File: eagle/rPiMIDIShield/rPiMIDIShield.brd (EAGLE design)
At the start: 56 x 85 mm, 9 parts

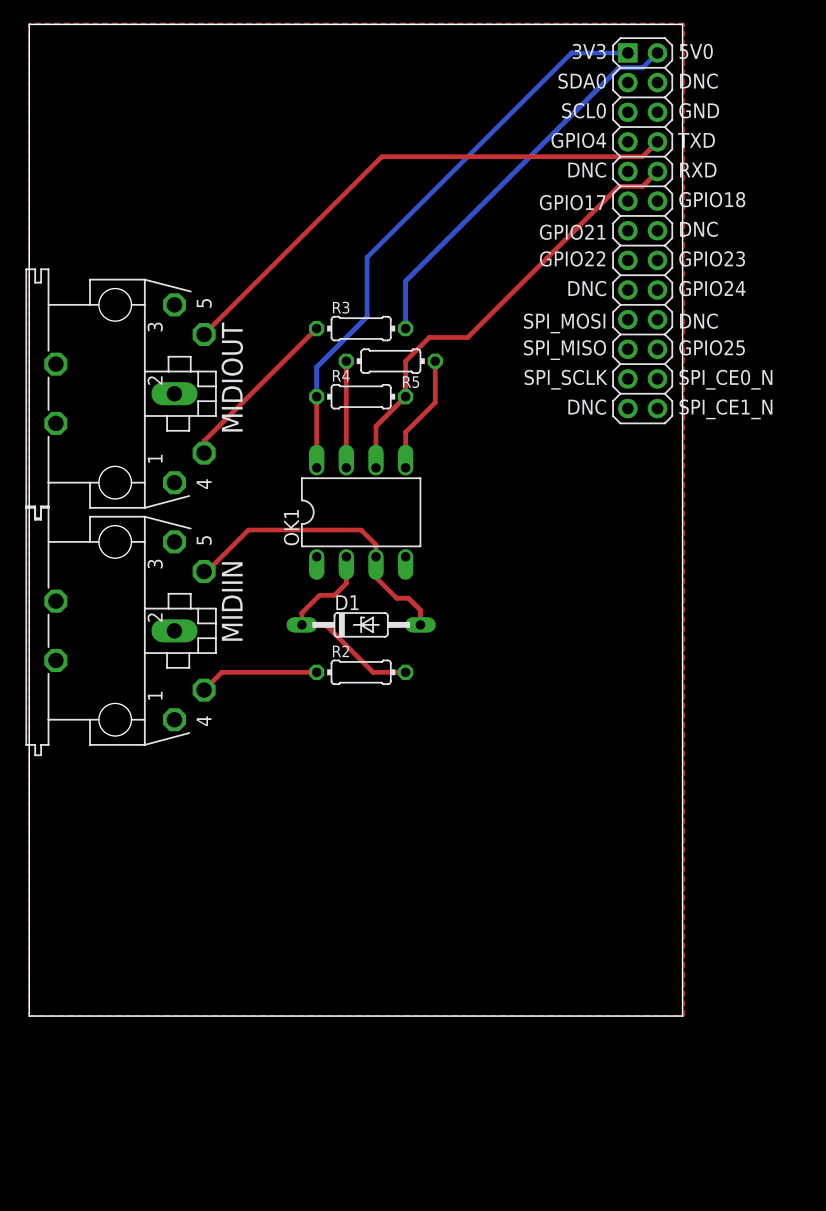
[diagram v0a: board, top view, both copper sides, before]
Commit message: Added GPIO headers to the rPI board
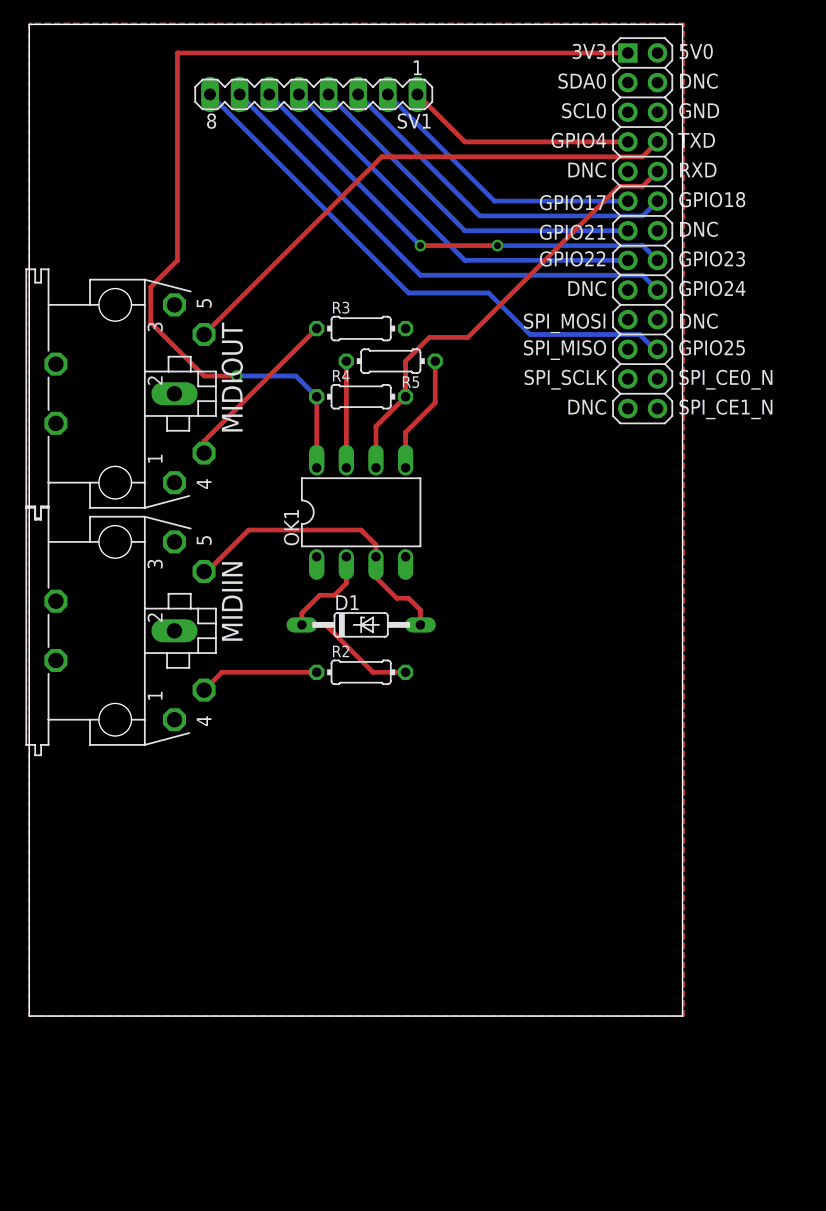
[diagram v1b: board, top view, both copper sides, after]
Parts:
- added SV1: (no value), con-lstb:MA08-1
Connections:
- net GPIO17: now also SV1.2
- net GPIO18: now also SV1.3
- net GPIO21: now also SV1.4
- net GPIO22: now also SV1.5
- net GPIO23: now also SV1.6
- net GPIO24: now also SV1.7
- net GPIO25: now also SV1.8
- net GPIO4: now also SV1.1
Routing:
- net GPIO25: track 0.00 -> 47.4 mm
- net GPIO24: track 0.00 -> 42.8 mm
- net GPIO23: track 0.00 -> 39.2 mm, vias 0 -> 2
- net 3.3V: track 49.2 -> 85.4 mm, vias 0 -> 1
- net GPIO22: track 0.00 -> 34.1 mm
- net 5.0V: track 33.8 -> 0.00 mm
- net GPIO18: track 0.00 -> 30.5 mm
- net GPIO21: track 0.00 -> 30.5 mm
- net GPIO17: track 0.00 -> 24.4 mm
- net GPIO4: track 0.00 -> 19.5 mm
- added copper zone on layer 16, net 5.0V
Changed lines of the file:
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@@
 <element name="R5" library="resistor" package="0204/7" value="1k" x="30.988" y="56.134" rot="R180"/>
 <element name="D1" library="diode" package="DO35Z10" value="1N821" x="28.448" y="33.528"/>
+<element name="SV1" library="con-lstb" package="MA08-1" value="" x="24.384" y="78.994" rot="R180">
+<attribute name="OC_NEWARK" value="unknown" x="24.384" y="78.994" size="1.778" layer="27" rot="R180" display="off"/>
+<attribute name="MPN" value="" x="24.384" y="78.994" size="1.778" layer="27" rot="R180" display="off"/>
+<attribute name="MF" value="" x="24.384" y="78.994" size="1.778" layer="27" rot="R180" display="off"/>
+<attribute name="OC_FARNELL" value="unknown" x="24.384" y="78.994" size="1.778" layer="27" rot="R180" display="off"/>
+</element>
 </elements>
 <signals>
 <signal name="GPIO17">
 <contactref element="U$1" pad="11"/>
+<contactref element="SV1" pad="2"/>
+<wire x1="51.308" y1="69.85" x2="39.878" y2="69.85" width="0.4064" layer="16"/>
+<wire x1="39.878" y1="69.85" x2="30.734" y2="78.994" width="0.4064" layer="16"/>
 </signal>
 <signal name="GPIO18">
 <contactref element="U$1" pad="12"/>
+<contactref element="SV1" pad="3"/>
+<wire x1="53.848" y1="69.85" x2="52.578" y2="68.58" width="0.4064" layer="16"/>
+<wire x1="52.578" y1="68.58" x2="38.608" y2="68.58" width="0.4064" layer="16"/>
+<wire x1="38.608" y1="68.58" x2="28.194" y2="78.994" width="0.4064" layer="16"/>
 </signal>
 <signal name="GPIO21">
 <contactref element="U$1" pad="13"/>
+<contactref element="SV1" pad="4"/>
+<wire x1="51.308" y1="67.31" x2="37.338" y2="67.31" width="0.4064" layer="16"/>
+<wire x1="37.338" y1="67.31" x2="25.654" y2="78.994" width="0.4064" layer="16"/>
 </signal>
 <signal name="GPIO22">
 <contactref element="U$1" pad="15"/>
+<contactref element="SV1" pad="5"/>
+<wire x1="51.308" y1="64.77" x2="37.338" y2="64.77" width="0.4064" layer="16"/>
+<wire x1="37.338" y1="64.77" x2="23.114" y2="78.994" width="0.4064" layer="16"/>
 </signal>
 <signal name="GPIO23">
 <contactref element="U$1" pad="16"/>
+<contactref element="SV1" pad="6"/>
+<wire x1="53.848" y1="64.77" x2="52.578" y2="66.04" width="0.4064" layer="16"/>
+<wire x1="52.578" y1="66.04" x2="40.132" y2="66.04" width="0.4064" layer="16"/>
+<via x="40.132" y="66.04" extent="1-16" drill="0.6" shape="square"/>
+<wire x1="40.132" y1="66.04" x2="33.528" y2="66.04" width="0.4064" layer="1"/>
+<via x="33.528" y="66.04" extent="1-16" drill="0.6" shape="square"/>
+<wire x1="33.528" y1="66.04" x2="20.574" y2="78.994" width="0.4064" layer="16"/>
 </signal>
 <signal name="GPIO24">
 <contactref element="U$1" pad="18"/>
+<contactref element="SV1" pad="7"/>
+<wire x1="53.848" y1="62.23" x2="52.578" y2="63.5" width="0.4064" layer="16"/>
+<wire x1="52.578" y1="63.5" x2="33.528" y2="63.5" width="0.4064" layer="16"/>
+<wire x1="33.528" y1="63.5" x2="18.034" y2="78.994" width="0.4064" layer="16"/>
 </signal>
 <signal name="GPIO25">
 <contactref element="U$1" pad="22"/>
+<contactref element="SV1" pad="8"/>
+<wire x1="53.848" y1="57.15" x2="53.594" y2="57.15" width="0.4064" layer="16"/>
+<wire x1="53.594" y1="57.15" x2="52.324" y2="58.42" width="0.4064" layer="16"/>
+<wire x1="52.324" y1="58.42" x2="42.926" y2="58.42" width="0.4064" layer="16"/>
+<wire x1="42.926" y1="58.42" x2="39.37" y2="61.976" width="0.4064" layer="16"/>
+<wire x1="39.37" y1="61.976" x2="32.512" y2="61.976" width="0.4064" layer="16"/>
+<wire x1="32.512" y1="61.976" x2="15.494" y2="78.994" width="0.4064" layer="16"/>
 </signal>
 <signal name="GPIO4">
 <contactref element="U$1" pad="7"/>
+<contactref element="SV1" pad="1"/>
+<wire x1="51.054" y1="74.93" x2="37.338" y2="74.93" width="0.4064" layer="1"/>
+<wire x1="37.338" y1="74.93" x2="33.274" y2="78.994" width="0.4064" layer="1"/>
+<wire x1="51.054" y1="74.93" x2="51.308" y2="74.93" width="0" layer="19" extent="1-1"/>
 </signal>
 <signal name="3.3V">
@@
 <contactref element="OK1" pad="8"/>
 <wire x1="24.638" y1="53.086" x2="24.638" y2="47.244" width="0.4064" layer="1"/>
-<wire x1="24.638" y1="53.086" x2="24.638" y2="55.626" width="0.4064" layer="16"/>
-<wire x1="24.638" y1="55.626" x2="28.956" y2="59.944" width="0.4064" layer="16"/>
-<wire x1="28.956" y1="59.944" x2="28.956" y2="65.024" width="0.4064" layer="16"/>
-<wire x1="28.956" y1="65.024" x2="46.482" y2="82.55" width="0.4064" layer="16"/>
-<wire x1="46.482" y1="82.55" x2="51.308" y2="82.55" width="0.4064" layer="16"/>
+<wire x1="51.308" y1="82.55" x2="12.7" y2="82.55" width="0.4064" layer="1"/>
+<wire x1="12.7" y1="82.55" x2="12.7" y2="64.77" width="0.4064" layer="1"/>
+<wire x1="12.7" y1="64.77" x2="10.414" y2="62.484" width="0.4064" layer="1"/>
+<wire x1="10.414" y1="62.484" x2="10.414" y2="59.436" width="0.4064" layer="1"/>
+<wire x1="10.414" y1="59.436" x2="14.986" y2="54.864" width="0.4064" layer="1"/>
+<wire x1="14.986" y1="54.864" x2="17.78" y2="54.864" width="0.4064" layer="1"/>
+<via x="17.78" y="54.864" extent="1-16" drill="0.6" shape="square"/>
+<wire x1="17.78" y1="54.864" x2="22.86" y2="54.864" width="0.4064" layer="16"/>
+<wire x1="22.86" y1="54.864" x2="24.638" y2="53.086" width="0.4064" layer="16"/>
 <wire x1="24.638" y1="47.244" x2="24.638" y2="46.99" width="0" layer="19" extent="1-1"/>
 </signal>
@@
 <contactref element="U$1" pad="2"/>
 <contactref element="R3" pad="2"/>
-<wire x1="53.848" y1="82.55" x2="52.578" y2="81.28" width="0.4064" layer="16"/>
-<wire x1="52.578" y1="81.28" x2="50.546" y2="81.28" width="0.4064" layer="16"/>
-<wire x1="50.546" y1="81.28" x2="32.258" y2="62.992" width="0.4064" layer="16"/>
-<wire x1="32.258" y1="62.992" x2="32.258" y2="58.928" width="0.4064" layer="16"/>
+<polygon width="0.4064" layer="16">
+<vertex x="0" y="85.09"/>
+<vertex x="0" y="0"/>
+<vertex x="56.134" y="0"/>
+<vertex x="56.134" y="85.09"/>
+<vertex x="0.254" y="85.09"/>
+</polygon>
 </signal>
 <signal name="GND">

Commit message: Modified the labels so they don't show up on silkscreen. Also moved all components within eagle's 'Approved Board Size'
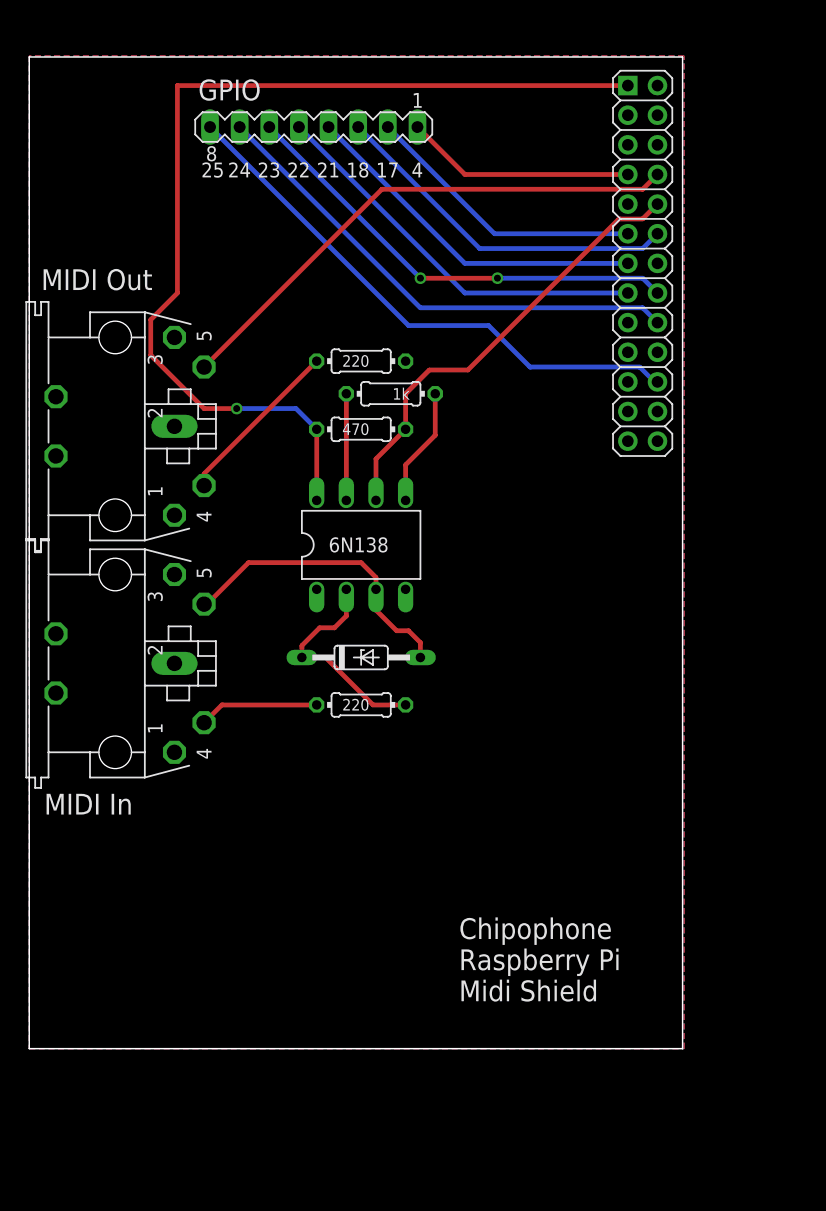
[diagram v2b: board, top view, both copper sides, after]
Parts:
- removed U$1: RASPBERRYPI_BB, microbuilder:RASBERRYPI_SHIELD
- added GPIO: RASPBERRYPI_BB, microbuilder:RASBERRYPI_SHIELD
- moved MIDIIN 2.79 mm to (7.37, 30.2)
- moved MIDIOUT 2.79 mm to (7.37, 50.5)
- moved D1 2.79 mm to (28.4, 30.7)
- moved OK1 2.79 mm to (28.4, 40.4)
- moved R2 2.79 mm to (28.4, 26.7)
- moved R3 2.79 mm to (28.4, 56.1)
- moved R4 2.79 mm to (28.4, 50.3)
- moved R5 2.79 mm to (31.0, 53.3)
- moved SV1 2.79 mm to (24.4, 76.2)
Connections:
- removed net PE: MIDIIN.PE, MIDIIN.PE@
- net 3.3V: now also GPIO.1; no longer U$1.1
- net 5.0V: now also GPIO.2; no longer U$1.2
- net GND: now also GPIO.6, MIDIIN.PE, MIDIIN.PE@, MIDIOUT.2; no longer U$1.6
- net GPIO17: now also GPIO.11; no longer U$1.11
- net GPIO18: now also GPIO.12; no longer U$1.12
- net GPIO21: now also GPIO.13; no longer U$1.13
- net GPIO22: now also GPIO.15; no longer U$1.15
- net GPIO23: now also GPIO.16; no longer U$1.16
- net GPIO24: now also GPIO.18; no longer U$1.18
- net GPIO25: now also GPIO.22; no longer U$1.22
- net GPIO4: now also GPIO.7; no longer U$1.7
- net MISO: now also GPIO.21; no longer U$1.21
- net MOSI: now also GPIO.19; no longer U$1.19
- net RXD: now also GPIO.10; no longer U$1.10
- net SCL: now also GPIO.5; no longer U$1.5
- net SCLK: now also GPIO.23; no longer U$1.23
- net SDA: now also GPIO.3; no longer U$1.3
- net SPI_CE0: now also GPIO.24; no longer U$1.24
- net SPI_CE1: now also GPIO.26; no longer U$1.26
- net TXD: now also GPIO.8; no longer U$1.8
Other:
- board text added: "17"
- board text added: "18"
- board text added: "21"
- board text added: "22"
- board text added: "23"
- board text added: "24"
- board text added: "25"
- board text added: "4"
- board text added: "Chipophone Raspberry Pi Midi Shield"
- board text added: "GPIO"
- board text added: "MIDI In"
- board text added: "MIDI Out"

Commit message: started adding switches for 5v power over MIDI
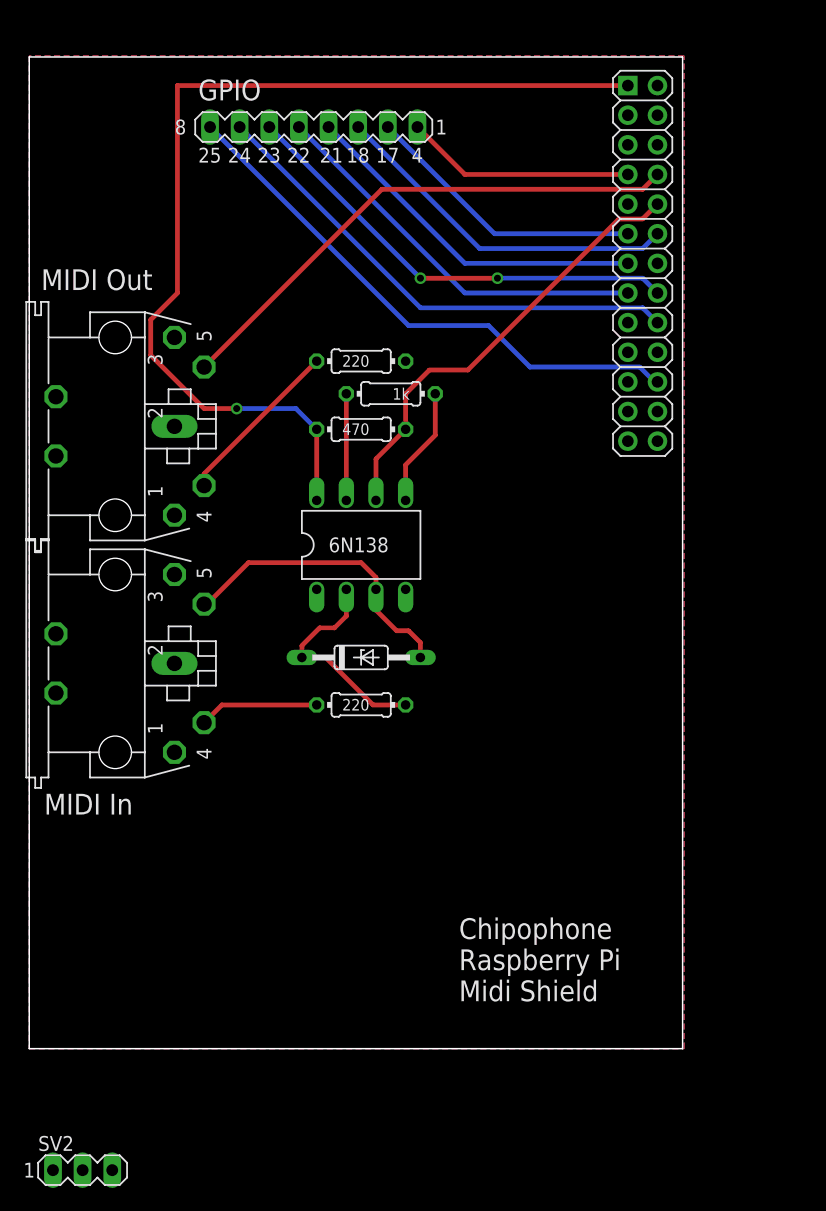
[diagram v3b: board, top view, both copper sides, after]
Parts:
- added SV2: (no value), con-lstb:MA03-1
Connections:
- new net N$2: SV2.2
- net 5.0V: now also SV2.1
- net GND: now also SV2.3
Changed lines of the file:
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@@
 <plain>
 <text x="14.478" y="78.486" size="1.778" layer="25">GPIO</text>
-<text x="14.732" y="71.882" size="1.27" layer="25">25</text>
-<text x="17.018" y="71.882" size="1.27" layer="25">24</text>
-<text x="19.558" y="71.882" size="1.27" layer="25">23</text>
-<text x="24.638" y="71.882" size="1.27" layer="25">21</text>
-<text x="27.178" y="71.882" size="1.27" layer="25">18</text>
-<text x="29.718" y="71.882" size="1.27" layer="25">17</text>
-<text x="32.766" y="71.882" size="1.27" layer="25">4</text>
-<text x="22.098" y="71.882" size="1.27" layer="25">22</text>
+<text x="14.478" y="73.152" size="1.27" layer="25">25</text>
+<text x="17.018" y="73.152" size="1.27" layer="25">24</text>
+<text x="19.558" y="73.152" size="1.27" layer="25">23</text>
+<text x="24.892" y="73.152" size="1.27" layer="25">21</text>
+<text x="27.178" y="73.152" size="1.27" layer="25">18</text>
+<text x="29.718" y="73.152" size="1.27" layer="25">17</text>
+<text x="32.766" y="73.152" size="1.27" layer="25">4</text>
+<text x="22.098" y="73.152" size="1.27" layer="25">22</text>
 <text x="1.27" y="17.272" size="1.778" layer="25">MIDI In</text>
 <text x="1.016" y="62.23" size="1.778" layer="25">MIDI Out</text>
@@
 <attribute name="VALUE" x="25.654" y="79.121" size="1.27" layer="27" ratio="10" rot="R180"/>
 </element>
+<element name="SV2" library="con-lstb" package="MA03-1" value="" x="4.572" y="-13.208">
+<attribute name="OC_NEWARK" value="unknown" x="4.572" y="-13.208" size="1.778" layer="27" display="off"/>
+<attribute name="MPN" value="" x="4.572" y="-13.208" size="1.778" layer="27" display="off"/>
+<attribute name="MF" value="" x="4.572" y="-13.208" size="1.778" layer="27" display="off"/>
+<attribute name="OC_FARNELL" value="unknown" x="4.572" y="-13.208" size="1.778" layer="27" display="off"/>
+</element>
 </elements>
 <signals>
@@
 <vertex x="56.134" y="82.296"/>
 </polygon>
+<contactref element="SV2" pad="1"/>
+<wire x1="32.258" y1="56.134" x2="2.032" y2="-13.208" width="0" layer="19" extent="1-1"/>
 </signal>
 <signal name="GND">
@@
 <contactref element="MIDIIN" pad="PE@"/>
 <contactref element="MIDIIN" pad="PE"/>
+<contactref element="SV2" pad="3"/>
+<wire x1="2.286" y1="27.686" x2="7.112" y2="-13.208" width="0" layer="19" extent="1-1"/>
 </signal>
 <signal name="SDA">
@@
 <wire x1="23.368" y1="30.734" x2="23.368" y2="30.988" width="0" layer="19" extent="1-1"/>
 </signal>
+<signal name="N$2">
+<contactref element="SV2" pad="2"/>
+</signal>
 </signals>
